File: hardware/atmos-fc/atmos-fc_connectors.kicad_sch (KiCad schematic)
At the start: 29 parts, among them J1 Conn_01x04, J3 USB_C_Receptacle_USB2.0_16P, J4 Conn_01x03, J5 Conn_01x06, J6 Conn_01x06, J7 Conn_01x02, U8 USBLC6-2P6

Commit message: Initial commit
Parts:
- J1, J4, J5, J6, J7: now left out of the parts list
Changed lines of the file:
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@@
 		(unit 1)
 		(exclude_from_sim no)
-		(in_bom yes)
+		(in_bom no)
 		(on_board yes)
 		(dnp no)
@@
 		(unit 1)
 		(exclude_from_sim no)
-		(in_bom yes)
+		(in_bom no)
 		(on_board yes)
 		(dnp no)
@@
 		(unit 1)
 		(exclude_from_sim no)
-		(in_bom yes)
+		(in_bom no)
 		(on_board yes)
 		(dnp no)
@@
 		(unit 1)
 		(exclude_from_sim no)
-		(in_bom yes)
+		(in_bom no)
 		(on_board yes)
 		(dnp no)
@@
 		(unit 1)
 		(exclude_from_sim no)
-		(in_bom yes)
+		(in_bom no)
 		(on_board yes)
 		(dnp no)

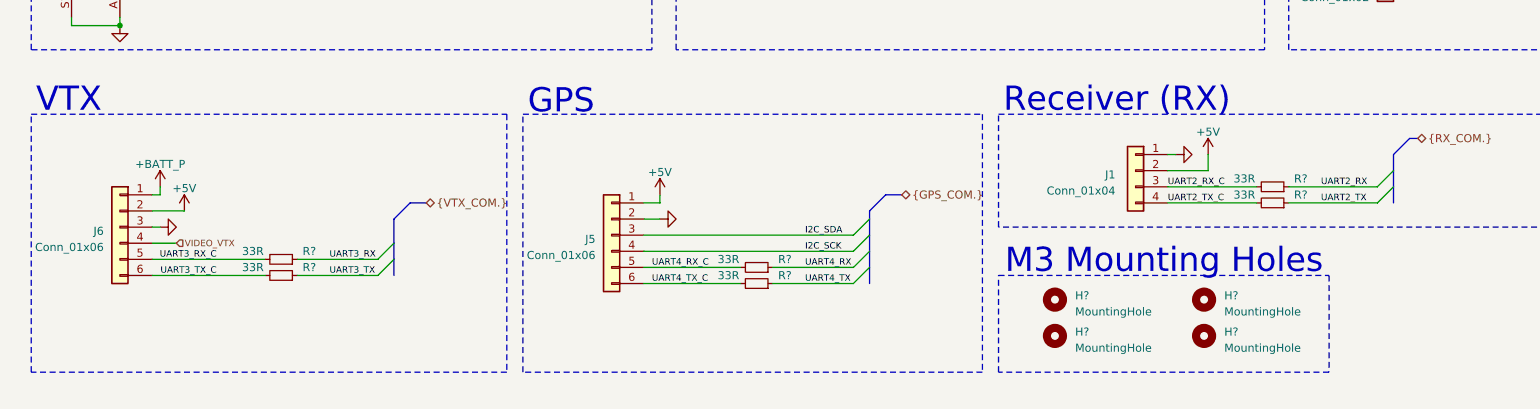
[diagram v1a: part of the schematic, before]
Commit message: Improved layout
Added oversized holes for mounting silicone inserts and improved layout.
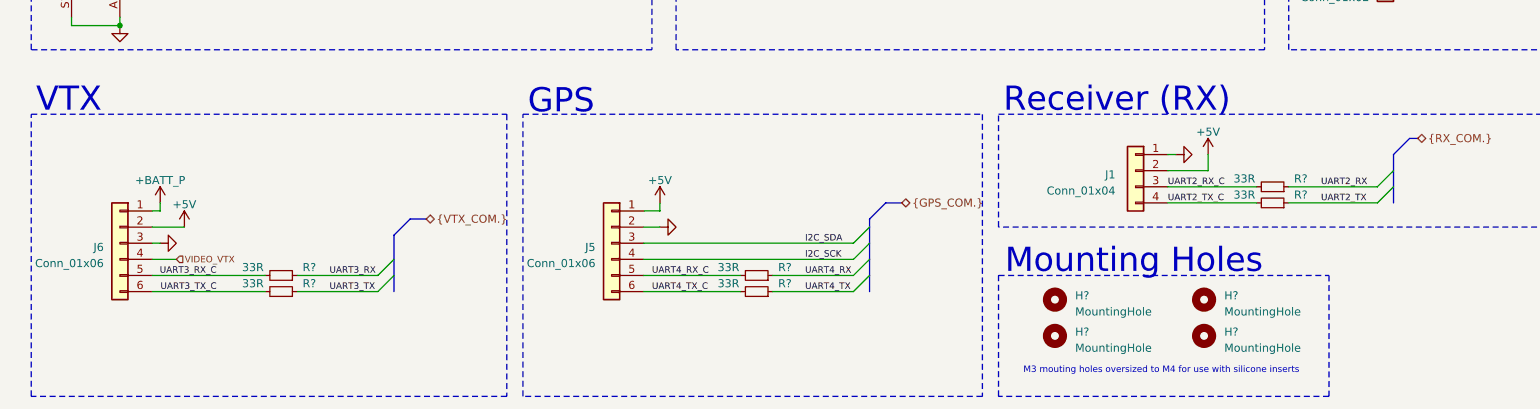
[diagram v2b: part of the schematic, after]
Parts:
- H? (x4): footprint MountingHole:MountingHole_3.2mm_M3 -> MountingHole:MountingHole_4.3mm_M4
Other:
- note added: "M3 mouting holes oversized to M4 for use with silicone inserts"
- note added: "Mounting Holes"
- note removed: "M3 Mounting Holes"
- moved on the sheet: J5, J6, R?

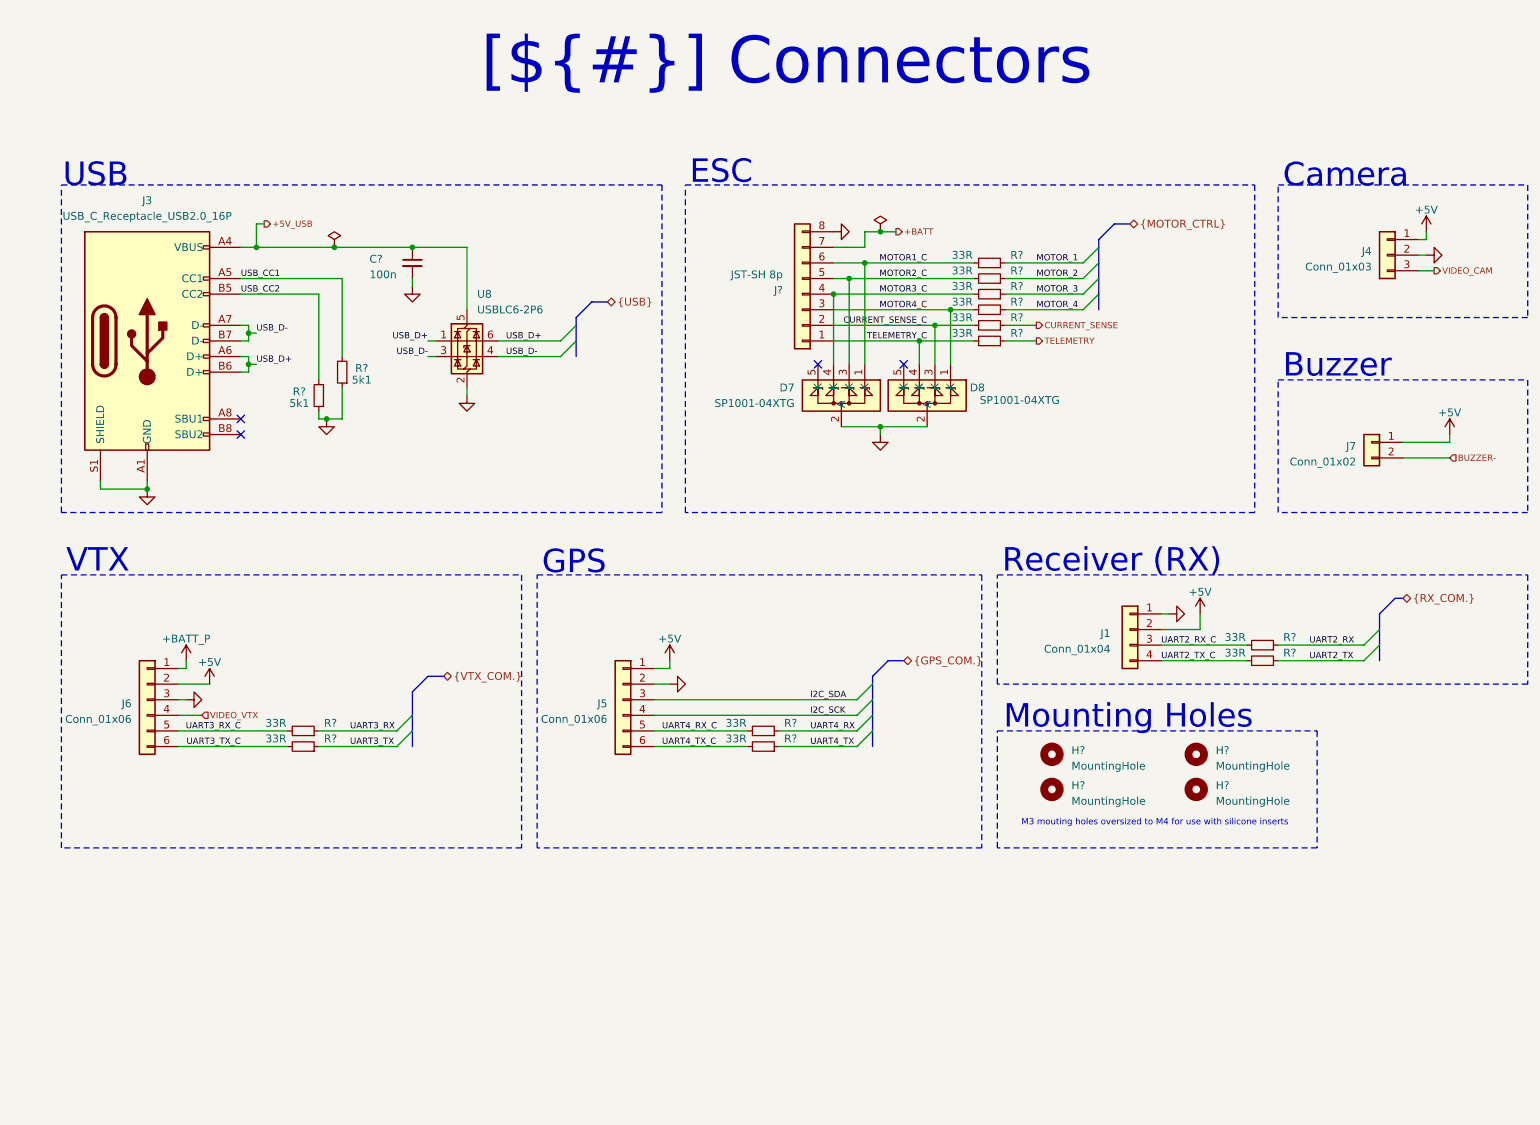
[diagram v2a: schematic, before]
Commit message: Add soldering pads for ESC
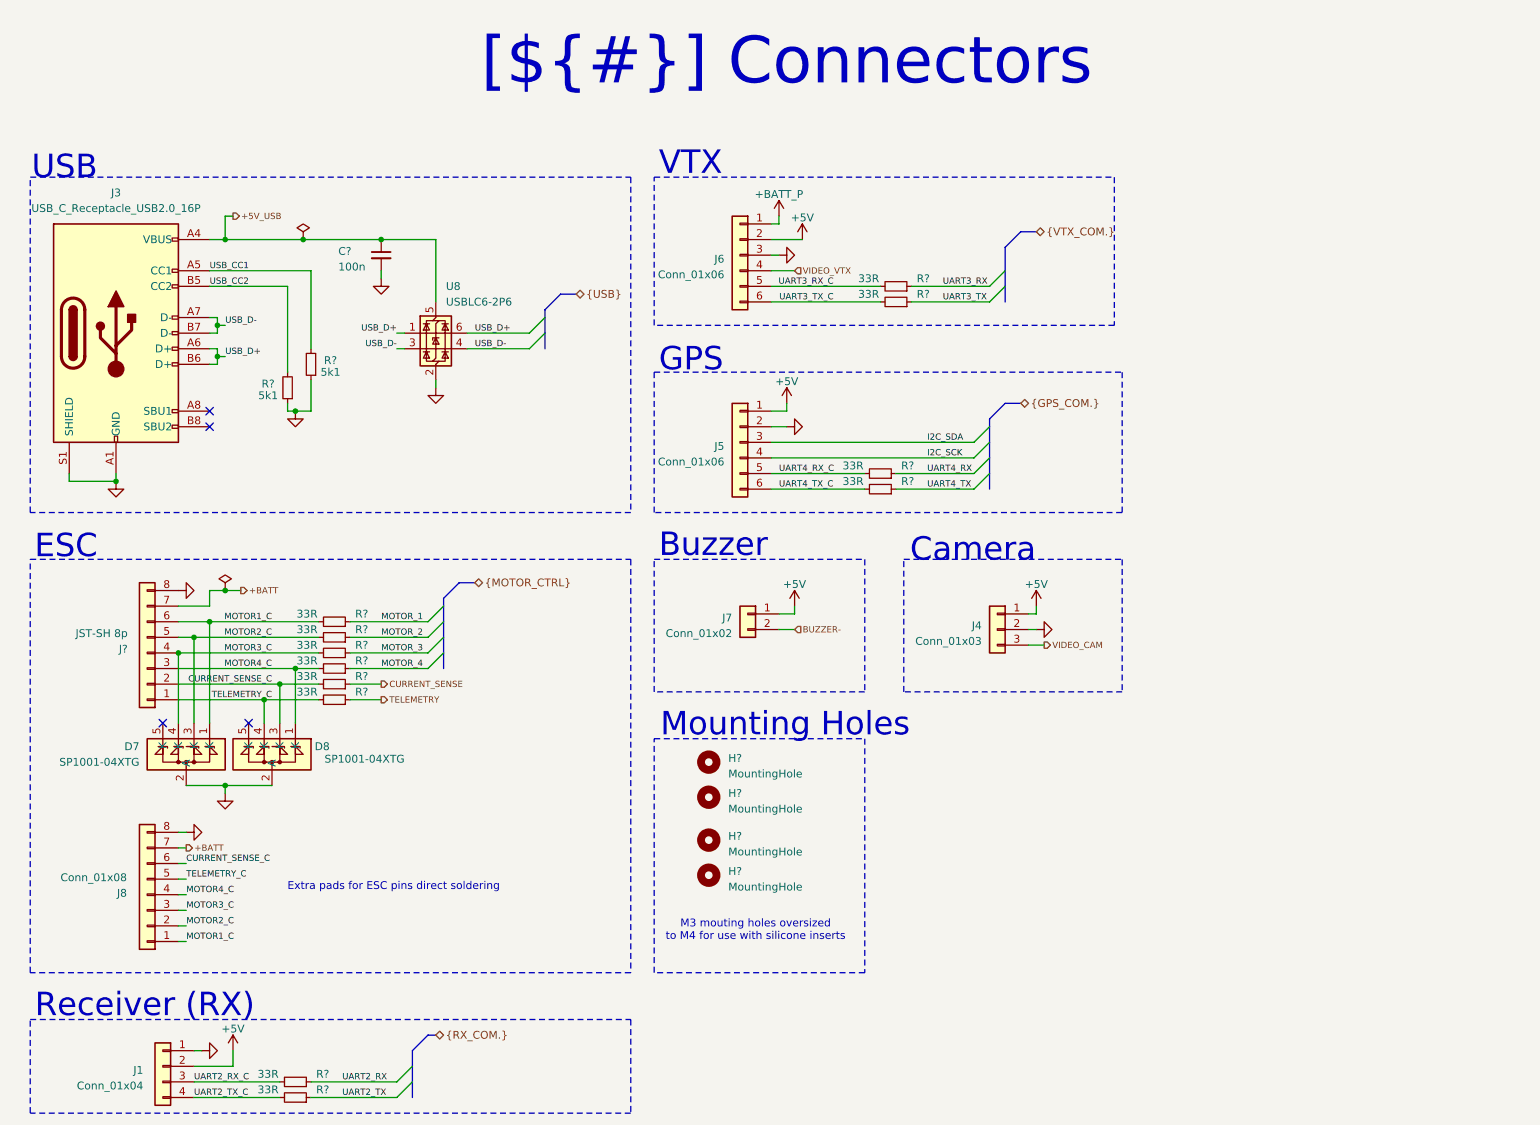
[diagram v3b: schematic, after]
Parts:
- added J8: Conn_01x08, 0_connector:SolderWirePads-2x4, symbol Connector_Generic:Conn_01x08
- J1: footprint 0_connector:SolderWirePads-2x4 -> 0_connector:SolderWirePads-2x2
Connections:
- net +BATT: now also J8.7 (Pin_7)
- net CURRENT_SENSE_C: now also J8.6 (Pin_6)
- net GND: now also J8.8 (Pin_8)
- net MOTOR1_C: now also J8.1 (Pin_1)
- net MOTOR2_C: now also J8.2 (Pin_2)
- net MOTOR3_C: now also J8.3 (Pin_3)
- net MOTOR4_C: now also J8.4 (Pin_4)
- net TELEMETRY_C: now also J8.5 (Pin_5)
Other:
- note added: "Extra pads for ESC pins direct soldering"
- moved on the sheet: C?, D7, D8, H?, J1, J3, J4, J5, J6, J7, J?, R?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

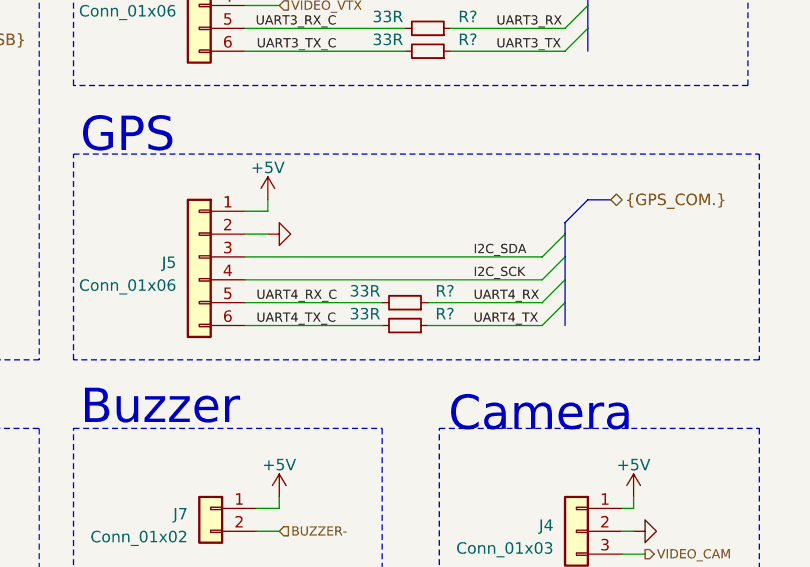
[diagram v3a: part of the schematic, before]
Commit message: Added 100n on ADC inputs and improved layout
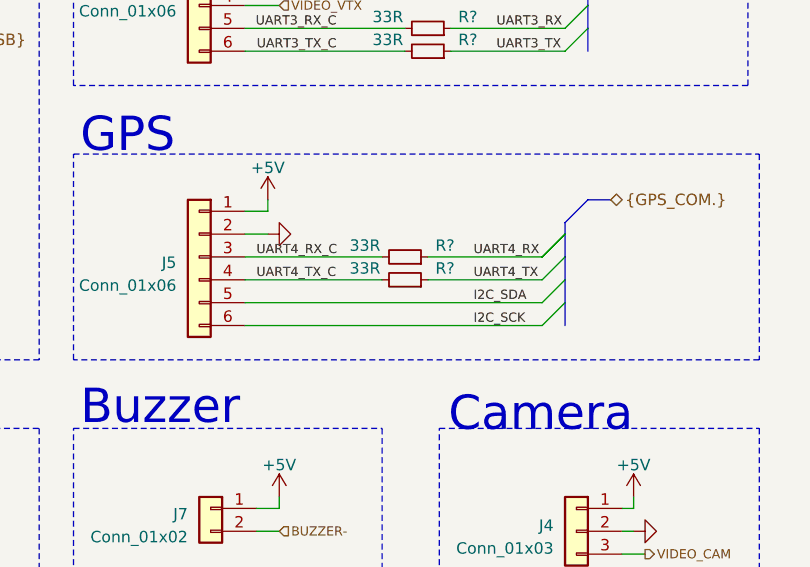
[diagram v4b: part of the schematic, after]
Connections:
- net I2C_SCK: now also J5.6 (Pin_6); no longer J5.4 (Pin_4)
- net I2C_SDA: now also J5.5 (Pin_5); no longer J5.3 (Pin_3)
- net UART4_RX_C: now also J5.3 (Pin_3); no longer J5.5 (Pin_5)
- net UART4_TX_C: now also J5.4 (Pin_4); no longer J5.6 (Pin_6)
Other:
- moved on the sheet: R?
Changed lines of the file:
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@@
 	)
 	(bus_entry
-		(at 181.61 87.63)
+		(at 181.61 82.55)
 		(size -2.54 2.54)
 		(stroke
@@
 		)
 	)
+	(bus_entry
+		(at 181.61 87.63)
+		(size -2.54 2.54)
+		(stroke
+			(width 0)
+			(type default)
+		)
+	)
 	(bus
 		(pts
@@
 	(wire
 		(pts
+			(xy 146.05 87.63) (xy 161.29 87.63)
+		)
+		(stroke
+			(width 0)
+			(type default)
+		)
+	)
+	(wire
+		(pts
 			(xy 147.32 54.61) (xy 146.05 54.61)
 		)
@@
 	(wire
 		(pts
+			(xy 146.05 90.17) (xy 179.07 90.17)
+		)
+		(stroke
+			(width 0)
+			(type default)
+		)
+	)
+	(wire
+		(pts
 			(xy 77.47 124.46) (xy 82.55 124.46)
 		)
@@
 	(wire
 		(pts
+			(xy 166.37 87.63) (xy 179.07 87.63)
+		)
+		(stroke
+			(width 0)
+			(type default)
+		)
+	)
+	(wire
+		(pts
 			(xy 54.61 114.3) (xy 49.53 114.3)
 		)
@@
 	(wire
 		(pts
-			(xy 149.86 113.03) (xy 147.32 113.03)
+			(xy 146.05 85.09) (xy 161.29 85.09)
 		)
 		(stroke
@@
 	(wire
 		(pts
-			(xy 49.53 111.76) (xy 54.61 111.76)
+			(xy 149.86 113.03) (xy 147.32 113.03)
 		)
 		(stroke
@@
 	(wire
 		(pts
-			(xy 71.12 189.23) (xy 85.09 189.23)
+			(xy 49.53 111.76) (xy 54.61 111.76)
 		)
 		(stroke
@@
 	(wire
 		(pts
-			(xy 146.05 87.63) (xy 179.07 87.63)
+			(xy 71.12 189.23) (xy 85.09 189.23)
 		)
 		(stroke
@@
 		)
 	)
-	(wire
+	(bus
 		(pts
-			(xy 55.88 66.04) (xy 57.15 66.04)
+			(xy 181.61 85.09) (xy 181.61 87.63)
 		)
 		(stroke
@@
 	(wire
 		(pts
-			(xy 57.15 140.97) (xy 57.15 142.24)
+			(xy 55.88 66.04) (xy 57.15 66.04)
 		)
 		(stroke
@@
 	(wire
 		(pts
-			(xy 55.88 71.12) (xy 55.88 69.85)
+			(xy 57.15 140.97) (xy 57.15 142.24)
 		)
 		(stroke
@@
 		)
 	)
-	(wire
+	(bus
 		(pts
-			(xy 49.53 127) (xy 63.5 127)
+			(xy 181.61 87.63) (xy 181.61 90.17)
 		)
 		(stroke
@@
 		)
 	)
-	(bus
+	(wire
 		(pts
-			(xy 181.61 90.17) (xy 181.61 92.71)
+			(xy 55.88 71.12) (xy 55.88 69.85)
 		)
 		(stroke
@@
 	(wire
 		(pts
-			(xy 82.55 58.42) (xy 82.55 57.15)
+			(xy 49.53 127) (xy 63.5 127)
 		)
 		(stroke
@@
 		)
 	)
-	(wire
+	(bus
 		(pts
-			(xy 49.53 124.46) (xy 66.04 124.46)
+			(xy 181.61 90.17) (xy 181.61 92.71)
 		)
 		(stroke
@@
 		)
 	)
-	(bus
+	(wire
 		(pts
-			(xy 181.61 82.55) (xy 181.61 85.09)
+			(xy 82.55 58.42) (xy 82.55 57.15)
 		)
 		(stroke
@@
 	(wire
 		(pts
-			(xy 31.75 90.17) (xy 31.75 91.44)
+			(xy 49.53 124.46) (xy 66.04 124.46)
 		)
 		(stroke
@@
 	(wire
 		(pts
-			(xy 49.53 121.92) (xy 68.58 121.92)
+			(xy 31.75 90.17) (xy 31.75 91.44)
 		)
 		(stroke
@@
 	(wire
 		(pts
-			(xy 146.05 92.71) (xy 161.29 92.71)
+			(xy 49.53 121.92) (xy 68.58 121.92)
 		)
 		(stroke
@@
 	(bus
 		(pts
-			(xy 181.61 87.63) (xy 181.61 90.17)
+			(xy 181.61 82.55) (xy 181.61 85.09)
 		)
 		(stroke
@@
 		)
 	)
-	(bus
-		(pts
-			(xy 181.61 85.09) (xy 181.61 87.63)
-		)
-		(stroke
-			(width 0)
-			(type default)
-		)
-	)
 	(wire
 		(pts
@@
 	(wire
 		(pts
-			(xy 166.37 92.71) (xy 179.07 92.71)
-		)
-		(stroke
-			(width 0)
-			(type default)
-		)
-	)
-	(wire
-		(pts
 			(xy 49.53 148.59) (xy 50.8 148.59)
 		)
@@
 	(wire
 		(pts
-			(xy 166.37 90.17) (xy 179.07 90.17)
+			(xy 166.37 85.09) (xy 179.07 85.09)
 		)
 		(stroke
@@
 	(wire
 		(pts
-			(xy 146.05 85.09) (xy 179.07 85.09)
-		)
-		(stroke
-			(width 0)
-			(type default)
-		)
-	)
-	(wire
-		(pts
 			(xy 187.96 115.57) (xy 189.23 115.57)
 		)
@@
 	(wire
 		(pts
-			(xy 58.42 186.69) (xy 58.42 184.15)
+			(xy 146.05 92.71) (xy 179.07 92.71)
 		)
 		(stroke
@@
 	(wire
 		(pts
-			(xy 146.05 90.17) (xy 161.29 90.17)
+			(xy 58.42 186.69) (xy 58.42 184.15)
 		)
 		(stroke
@@
 	)
 	(label "I2C_SCK"
-		(at 171.45 87.63 0)
+		(at 171.45 92.71 0)
 		(fields_autoplaced yes)
 		(effects
@@
 	)
 	(label "I2C_SDA"
-		(at 171.45 85.09 0)
+		(at 171.45 90.17 0)
 		(fields_autoplaced yes)
 		(effects
@@
 	)
 	(label "UART4_RX"
-		(at 171.45 90.17 0)
+		(at 171.45 85.09 0)
 		(fields_autoplaced yes)
 		(effects
@@
 	)
 	(label "UART4_TX_C"
-		(at 147.32 92.71 0)
+		(at 147.32 87.63 0)
 		(fields_autoplaced yes)
 		(effects
@@
 	)
 	(label "UART4_TX"
-		(at 171.45 92.71 0)
+		(at 171.45 87.63 0)
 		(fields_autoplaced yes)
 		(effects
@@
 	)
 	(label "UART4_RX_C"
-		(at 147.32 90.17 0)
+		(at 147.32 85.09 0)
 		(fields_autoplaced yes)
 		(effects
@@
 	(symbol
 		(lib_id "Device:R_Small")
-		(at 163.83 92.71 270)
+		(at 163.83 87.63 270)
 		(mirror x)
 		(unit 1)
@@
 		(dnp no)
 		(property "Reference" "R?"
-			(at 168.275 91.44 90)
+			(at 168.275 86.36 90)
 			(effects
 				(font
@@
 		)
 		(property "Value" "33R"
-			(at 159.385 91.44 90)
+			(at 159.385 86.36 90)
 			(effects
 				(font
@@
 		)
 		(property "Footprint" "Resistor_SMD:R_0402_1005Metric"
-			(at 163.83 92.71 0)
+			(at 163.83 87.63 0)
 			(effects
 				(font
@@
 		)
 		(property "Datasheet" "~"
-			(at 163.83 92.71 0)
+			(at 163.83 87.63 0)
 			(effects
 				(font
@@
 		)
 		(property "Description" "Thick Film Resistors - SMD 1/16watt 33ohms 1% 100ppm"
-			(at 163.83 92.71 0)
+			(at 163.83 87.63 0)
 			(effects
 				(font
@@
 		)
 		(property "Manufacturer" "Vishay / Dale"
-			(at 163.83 92.71 0)
+			(at 163.83 87.63 0)
 			(effects
 				(font
@@
 		)
 		(property "Mfr Part Number" "CRCW040220K0FKED"
-			(at 163.83 92.71 0)
+			(at 163.83 87.63 0)
 			(effects
 				(font
@@
 	(symbol
 		(lib_id "Device:R_Small")
-		(at 163.83 90.17 270)
+		(at 163.83 85.09 270)
 		(mirror x)
 		(unit 1)
@@
 		(dnp no)
 		(property "Reference" "R?"
-			(at 168.275 88.9 90)
+			(at 168.275 83.82 90)
 			(effects
 				(font
@@
 		)
 		(property "Value" "33R"
-			(at 159.385 88.9 90)
+			(at 159.385 83.82 90)
 			(effects
 				(font
@@
 		)
 		(property "Footprint" "Resistor_SMD:R_0402_1005Metric"
-			(at 163.83 90.17 0)
+			(at 163.83 85.09 0)
 			(effects
 				(font
@@
 		)
 		(property "Datasheet" "~"
-			(at 163.83 90.17 0)
+			(at 163.83 85.09 0)
 			(effects
 				(font
@@
 		)
 		(property "Description" "Thick Film Resistors - SMD 1/16watt 33ohms 1% 100ppm"
-			(at 163.83 90.17 0)
+			(at 163.83 85.09 0)
 			(effects
 				(font
@@
 		)
 		(property "Manufacturer" "Vishay / Dale"
-			(at 163.83 90.17 0)
+			(at 163.83 85.09 0)
 			(effects
 				(font
@@
 		)
 		(property "Mfr Part Number" "CRCW040220K0FKED"
-			(at 163.83 90.17 0)
+			(at 163.83 85.09 0)
 			(effects
 				(font
